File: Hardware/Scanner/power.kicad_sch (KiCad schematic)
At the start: 15 parts, among them J1 I2C ThroughHole, J3 I2C, J4 Interface, U7 AP7312-1833W6-7

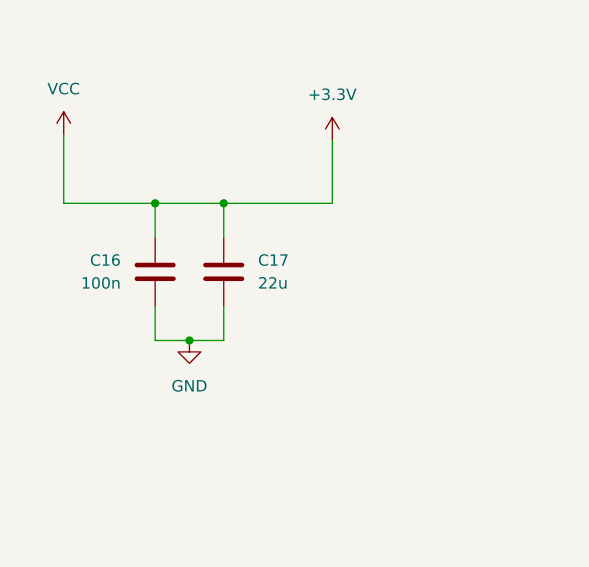
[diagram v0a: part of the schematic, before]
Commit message: Consistency of capacitor values
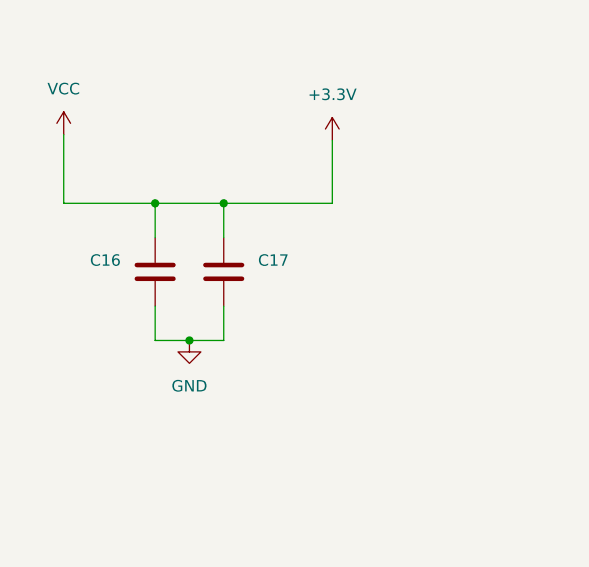
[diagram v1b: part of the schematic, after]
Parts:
- C16: value 100n -> (none)
- C17: value 22u -> (none)
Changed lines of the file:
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@@
       (effects (font (size 1.27 1.27)) (justify left))
     )
-    (property "Value" "22u" (id 1) (at 62.23 85.0899 0)
+    (property "Value" "" (id 1) (at 62.23 85.0899 0)
       (effects (font (size 1.27 1.27)) (justify left))
     )
@@
       (effects (font (size 1.27 1.27)) (justify right))
     )
-    (property "Value" "100n" (id 1) (at 46.99 85.0899 0)
+    (property "Value" "" (id 1) (at 46.99 85.0899 0)
       (effects (font (size 1.27 1.27)) (justify right))
     )

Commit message: LAtching circuit for controller board + minors
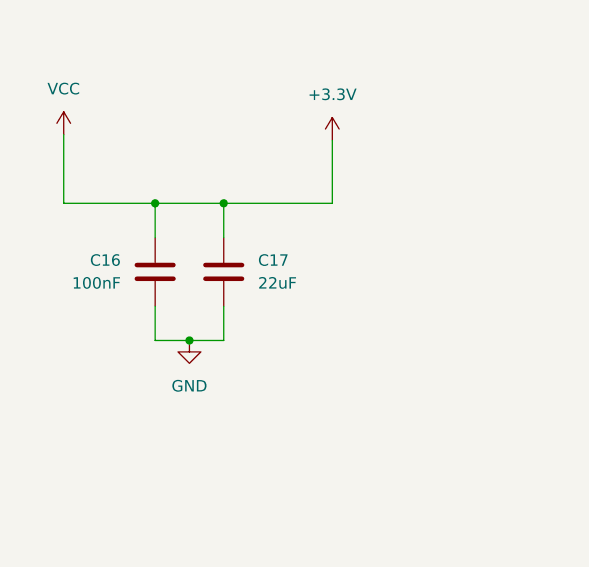
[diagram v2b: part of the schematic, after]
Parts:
- C16: value (none) -> 100nF
- C17: value (none) -> 22uF
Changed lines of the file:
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@@
       (effects (font (size 1.27 1.27)) (justify left))
     )
-    (property "Value" "" (id 1) (at 62.23 85.0899 0)
+    (property "Value" "22uF" (id 1) (at 62.23 85.0899 0)
       (effects (font (size 1.27 1.27)) (justify left))
     )
@@
       (effects (font (size 1.27 1.27)) (justify right))
     )
-    (property "Value" "" (id 1) (at 46.99 85.0899 0)
+    (property "Value" "100nF" (id 1) (at 46.99 85.0899 0)
       (effects (font (size 1.27 1.27)) (justify right))
     )
